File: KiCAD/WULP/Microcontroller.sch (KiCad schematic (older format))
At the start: 17 parts

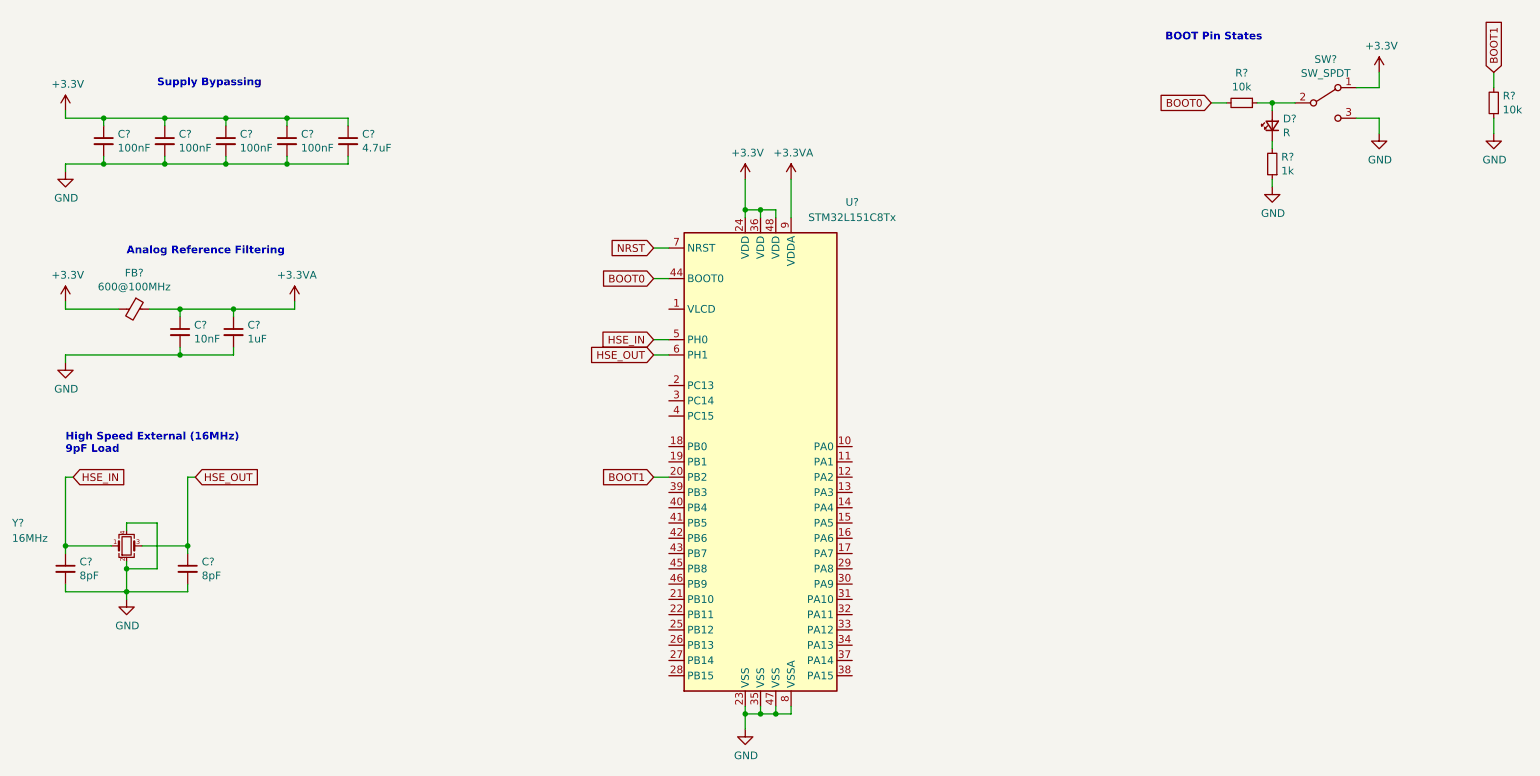
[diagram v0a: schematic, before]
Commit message: WULP sensor/connector updates
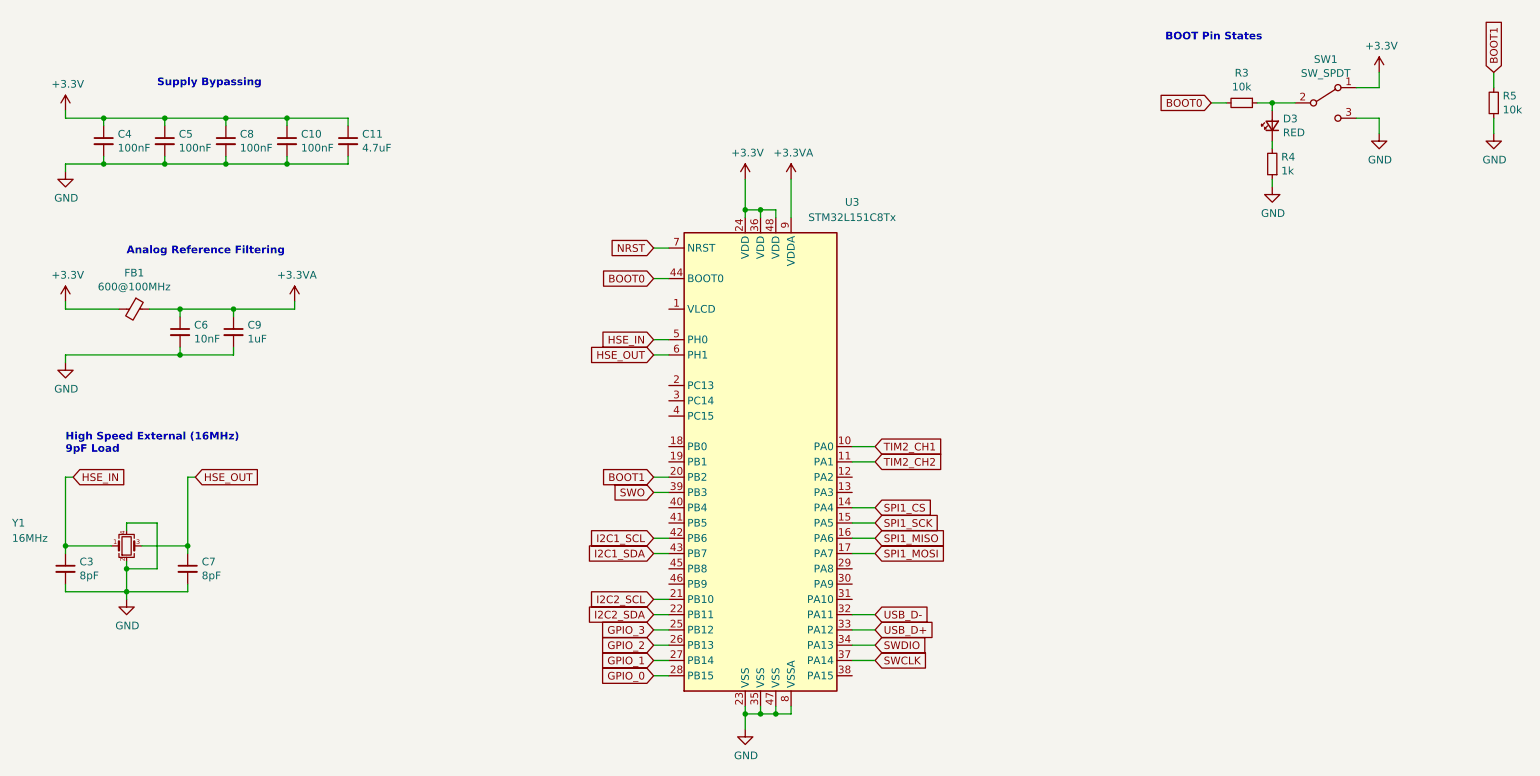
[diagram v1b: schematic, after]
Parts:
- D3: renamed from D?; value R -> RED
- SW1: renamed from SW?; footprint (none) -> Button_Switch_SMD:SW_SPDT_PCM12; LCSC (none) -> C431541
- gave numbers to parts that had none: 15
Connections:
- net TIM2_CH1: now reaches U3.10 (PA0)
- net TIM2_CH2: now reaches U3.11 (PA1)
- net SPI1_CS: now reaches U3.14 (PA4)
- net SPI1_SCK: now reaches U3.15 (PA5)
- net SPI1_MISO: now reaches U3.16 (PA6)
- net SPI1_MOSI: now reaches U3.17 (PA7)
- net I2C2_SCL: now reaches U3.21 (PB10)
- net I2C2_SDA: now reaches U3.22 (PB11)
- net GPIO_3: now reaches U3.25 (PB12)
- net GPIO_2: now reaches U3.26 (PB13)
- net GPIO_1: now reaches U3.27 (PB14)
- net GPIO_0: now reaches U3.28 (PB15)
- net USB_D-: now reaches U3.32 (PA11)
- net USB_D+: now reaches U3.33 (PA12)
- net SWDIO: now reaches U3.34 (PA13)
- net SWCLK: now reaches U3.37 (PA14)
- net SWO: now reaches U3.39 (PB3)
- net I2C1_SCL: now reaches U3.42 (PB6)
- net I2C1_SDA: now reaches U3.43 (PB7)
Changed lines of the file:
@@
 $Descr A4 11693 8268
 encoding utf-8
-Sheet 3 3
+Sheet 3 5
 Title ""
 Date ""
@@
 $EndDescr
 $Comp
-L MCU_ST_STM32L1:STM32L151C8Tx U?
+L MCU_ST_STM32L1:STM32L151C8Tx U3
 U 1 1 61B53E29
 P 5750 3450
-F 0 "U?" H 6350 5150 50  0000 C CNN
+F 0 "U3" H 6350 5150 50  0000 C CNN
 F 1 "STM32L151C8Tx" H 6350 5050 50  0000 C CNN
 F 2 "Package_QFP:LQFP-48_7x7mm_P0.5mm" H 5250 1950 50  0001 R CNN
@@
 $EndComp
 $Comp
-L Device:C_Small C?
+L Device:C_Small C4
 U 1 1 61B55765
 P 1450 1350
-F 0 "C?" H 1542 1396 50  0000 L CNN
+F 0 "C4" H 1542 1396 50  0000 L CNN
 F 1 "100nF" H 1542 1305 50  0000 L CNN
 F 2 "" H 1450 1350 50  0001 C CNN
@@
 $EndComp
 $Comp
-L Device:C_Small C?
+L Device:C_Small C5
 U 1 1 61B56E07
 P 1850 1350
-F 0 "C?" H 1942 1396 50  0000 L CNN
+F 0 "C5" H 1942 1396 50  0000 L CNN
 F 1 "100nF" H 1942 1305 50  0000 L CNN
 F 2 "" H 1850 1350 50  0001 C CNN
@@
 $EndComp
 $Comp
-L Device:C_Small C?
+L Device:C_Small C8
 U 1 1 61B57112
 P 2250 1350
-F 0 "C?" H 2342 1396 50  0000 L CNN
+F 0 "C8" H 2342 1396 50  0000 L CNN
 F 1 "100nF" H 2342 1305 50  0000 L CNN
 F 2 "" H 2250 1350 50  0001 C CNN
@@
 $EndComp
 $Comp
-L Device:C_Small C?
+L Device:C_Small C10
 U 1 1 61B572C5
 P 2650 1350
-F 0 "C?" H 2742 1396 50  0000 L CNN
+F 0 "C10" H 2742 1396 50  0000 L CNN
 F 1 "100nF" H 2742 1305 50  0000 L CNN
 F 2 "" H 2650 1350 50  0001 C CNN
@@
 $EndComp
 $Comp
-L Device:C_Small C?
+L Device:C_Small C11
 U 1 1 61B57637
 P 3050 1350
-F 0 "C?" H 3142 1396 50  0000 L CNN
+F 0 "C11" H 3142 1396 50  0000 L CNN
 F 1 "4.7uF" H 3142 1305 50  0000 L CNN
 F 2 "" H 3050 1350 50  0001 C CNN
@@
 $EndComp
 $Comp
-L power:+3.3V #PWR?
+L power:+3.3V #PWR0114
 U 1 1 61B57B0B
 P 1200 1150
-F 0 "#PWR?" H 1200 1000 50  0001 C CNN
+F 0 "#PWR0114" H 1200 1000 50  0001 C CNN
 F 1 "+3.3V" H 1215 1323 50  0000 C CNN
 F 2 "" H 1200 1150 50  0001 C CNN
@@
 $EndComp
 $Comp
-L power:GND #PWR?
+L power:GND #PWR0115
 U 1 1 61B58427
 P 1200 1550
-F 0 "#PWR?" H 1200 1300 50  0001 C CNN
+F 0 "#PWR0115" H 1200 1300 50  0001 C CNN
 F 1 "GND" H 1205 1377 50  0000 C CNN
 F 2 "" H 1200 1550 50  0001 C CNN
@@
 	1450 1500 1850 1500
 $Comp
-L power:+3.3V #PWR?
+L power:+3.3V #PWR0116
 U 1 1 61B59DEE
 P 5650 1600
-F 0 "#PWR?" H 5650 1450 50  0001 C CNN
+F 0 "#PWR0116" H 5650 1450 50  0001 C CNN
 F 1 "+3.3V" H 5665 1773 50  0000 C CNN
 F 2 "" H 5650 1600 50  0001 C CNN
@@
 Connection ~ 5750 1800
 $Comp
-L power:+3.3VA #PWR?
+L power:+3.3VA #PWR0117
 U 1 1 61B5BA93
 P 5950 1600
-F 0 "#PWR?" H 5950 1450 50  0001 C CNN
+F 0 "#PWR0117" H 5950 1450 50  0001 C CNN
 F 1 "+3.3VA" H 5965 1773 50  0000 C CNN
 F 2 "" H 5950 1600 50  0001 C CNN
@@
 	5950 1600 5950 1850
 $Comp
-L power:+3.3V #PWR?
+L power:+3.3V #PWR0118
 U 1 1 61B5C7AD
 P 1200 2400
-F 0 "#PWR?" H 1200 2250 50  0001 C CNN
+F 0 "#PWR0118" H 1200 2250 50  0001 C CNN
 F 1 "+3.3V" H 1215 2573 50  0000 C CNN
 F 2 "" H 1200 2400 50  0001 C CNN
@@
 $EndComp
 $Comp
-L power:GND #PWR?
+L power:GND #PWR0119
 U 1 1 61B5CCD8
 P 1200 2800
-F 0 "#PWR?" H 1200 2550 50  0001 C CNN
+F 0 "#PWR0119" H 1200 2550 50  0001 C CNN
 F 1 "GND" H 1205 2627 50  0000 C CNN
 F 2 "" H 1200 2800 50  0001 C CNN
@@
 $EndComp
 $Comp
-L Device:C_Small C?
+L Device:C_Small C6
 U 1 1 61B5D317
 P 1950 2600
-F 0 "C?" H 2042 2646 50  0000 L CNN
+F 0 "C6" H 2042 2646 50  0000 L CNN
 F 1 "10nF" H 2042 2555 50  0000 L CNN
 F 2 "" H 1950 2600 50  0001 C CNN
@@
 $EndComp
 $Comp
-L Device:C_Small C?
+L Device:C_Small C9
 U 1 1 61B5DC0A
 P 2300 2600
-F 0 "C?" H 2392 2646 50  0000 L CNN
+F 0 "C9" H 2392 2646 50  0000 L CNN
 F 1 "1uF" H 2392 2555 50  0000 L CNN
 F 2 "" H 2300 2600 50  0001 C CNN
@@
 $EndComp
 $Comp
-L power:+3.3VA #PWR?
+L power:+3.3VA #PWR0120
 U 1 1 61B5F121
 P 2700 2400
-F 0 "#PWR?" H 2700 2250 50  0001 C CNN
+F 0 "#PWR0120" H 2700 2250 50  0001 C CNN
 F 1 "+3.3VA" H 2715 2573 50  0000 C CNN
 F 2 "" H 2700 2400 50  0001 C CNN
@@
 $EndComp
 $Comp
-L Device:Ferrite_Bead_Small FB?
+L Device:Ferrite_Bead_Small FB1
 U 1 1 61B5FB4B
 P 1650 2450
-F 0 "FB?" V 1413 2450 50  0000 C CNN
+F 0 "FB1" V 1413 2450 50  0000 C CNN
 F 1 "600@100MHz" V 1504 2450 50  0000 C CNN
 F 2 "" V 1580 2450 50  0001 C CNN
@@
 	1950 2750 2300 2750
 $Comp
-L power:GND #PWR?
+L power:GND #PWR0121
 U 1 1 61B65960
 P 5650 5200
-F 0 "#PWR?" H 5650 4950 50  0001 C CNN
+F 0 "#PWR0121" H 5650 4950 50  0001 C CNN
 F 1 "GND" H 5655 5027 50  0000 C CNN
 F 2 "" H 5650 5200 50  0001 C CNN
@@
 Analog Reference Filtering
 $Comp
-L Device:Crystal_GND24_Small Y?
+L Device:Crystal_GND24_Small Y1
 U 1 1 61B82FD5
 P 1600 4000
-F 0 "Y?" H 850 4150 50  0000 L CNN
+F 0 "Y1" H 850 4150 50  0000 L CNN
 F 1 "16MHz" H 850 4050 50  0000 L CNN
 F 2 "Oscillator:Oscillator_SMD_SeikoEpson_SG8002CE-4Pin_3.2x2.5mm" H 1600 4000 50  0001 C CNN
@@
 	1600 4150 1600 4100
 $Comp
-L power:GND #PWR?
+L power:GND #PWR0122
 U 1 1 61B84FE3
 P 1600 4350
-F 0 "#PWR?" H 1600 4100 50  0001 C CNN
+F 0 "#PWR0122" H 1600 4100 50  0001 C CNN
 F 1 "GND" H 1605 4177 50  0000 C CNN
 F 2 "" H 1600 4350 50  0001 C CNN
@@
 	5050 2650 5150 2650
 $Comp
-L Device:C_Small C?
+L Device:C_Small C3
 U 1 1 61B8880B
 P 1200 4150
-F 0 "C?" H 1292 4196 50  0000 L CNN
+F 0 "C3" H 1292 4196 50  0000 L CNN
 F 1 "8pF" H 1292 4105 50  0000 L CNN
 F 2 "" H 1200 4150 50  0001 C CNN
@@
 $EndComp
 $Comp
-L Device:C_Small C?
+L Device:C_Small C7
 U 1 1 61B89170
 P 2000 4150
-F 0 "C?" H 2092 4196 50  0000 L CNN
+F 0 "C7" H 2092 4196 50  0000 L CNN
 F 1 "8pF" H 2092 4105 50  0000 L CNN
 F 2 "" H 2000 4150 50  0001 C CNN
@@
 	5150 3550 5050 3550
 $Comp
-L Switch:SW_SPDT SW?
+L Switch:SW_SPDT SW1
 U 1 1 61BA3EF0
 P 9450 1100
-F 0 "SW?" H 9450 1385 50  0000 C CNN
+F 0 "SW1" H 9450 1385 50  0000 C CNN
 F 1 "SW_SPDT" H 9450 1294 50  0000 C CNN
-F 2 "" H 9450 1100 50  0001 C CNN
+F 2 "Button_Switch_SMD:SW_SPDT_PCM12" H 9450 1100 50  0001 C CNN
 F 3 "~" H 9450 1100 50  0001 C CNN
+F 4 "C431541" H 9450 1100 50  0001 C CNN "LCSC"
 	1    9450 1100
 	1    0    0    -1
@@
 BOOT0
 $Comp
-L Device:R_Small R?
+L Device:R_Small R3
 U 1 1 61BA68DC
 P 8900 1100
-F 0 "R?" V 8704 1100 50  0000 C CNN
+F 0 "R3" V 8704 1100 50  0000 C CNN
 F 1 "10k" V 8795 1100 50  0000 C CNN
 F 2 "" H 8900 1100 50  0001 C CNN
@@
 	9000 1100 9100 1100
 $Comp
-L power:+3.3V #PWR?
+L power:+3.3V #PWR0123
 U 1 1 61BAA6FF
 P 9800 900
-F 0 "#PWR?" H 9800 750 50  0001 C CNN
+F 0 "#PWR0123" H 9800 750 50  0001 C CNN
 F 1 "+3.3V" H 9815 1073 50  0000 C CNN
 F 2 "" H 9800 900 50  0001 C CNN
@@
 $EndComp
 $Comp
-L power:GND #PWR?
+L power:GND #PWR0124
 U 1 1 61BAB201
 P 9800 1300
-F 0 "#PWR?" H 9800 1050 50  0001 C CNN
+F 0 "#PWR0124" H 9800 1050 50  0001 C CNN
 F 1 "GND" H 9805 1127 50  0000 C CNN
 F 2 "" H 9800 1300 50  0001 C CNN
@@
 BOOT1
 $Comp
-L Device:R_Small R?
+L Device:R_Small R5
 U 1 1 61BAF705
 P 10550 1100
-F 0 "R?" H 10491 1054 50  0000 R CNN
+F 0 "R5" H 10491 1054 50  0000 R CNN
 F 1 "10k" H 10491 1145 50  0000 R CNN
 F 2 "" H 10550 1100 50  0001 C CNN
@@
 $EndComp
 $Comp
-L power:GND #PWR?
+L power:GND #PWR0125
 U 1 1 61BAFAE7
 P 10550 1300
-F 0 "#PWR?" H 10550 1050 50  0001 C CNN
+F 0 "#PWR0125" H 10550 1050 50  0001 C CNN
 F 1 "GND" H 10555 1127 50  0000 C CNN
 F 2 "" H 10550 1300 50  0001 C CNN
@@
 	10550 1000 10550 900
 $Comp
-L Device:LED_Small D?
+L Device:LED_Small D3
 U 1 1 61BB391F
 P 9100 1250
-F 0 "D?" V 9146 1180 50  0000 R CNN
-F 1 "R" V 9055 1180 50  0000 R CNN
+F 0 "D3" V 9146 1180 50  0000 R CNN
+F 1 "RED" V 9055 1180 50  0000 R CNN
 F 2 "" V 9100 1250 50  0001 C CNN
 F 3 "~" V 9100 1250 50  0001 C CNN
@@
 $EndComp
 $Comp
-L Device:R_Small R?
+L Device:R_Small R4
 U 1 1 61BB464B
 P 9100 1500
-F 0 "R?" H 9041 1454 50  0000 R CNN
+F 0 "R4" H 9041 1454 50  0000 R CNN
 F 1 "1k" H 9041 1545 50  0000 R CNN
 F 2 "" H 9100 1500 50  0001 C CNN
@@
 $EndComp
 $Comp
-L power:GND #PWR?
+L power:GND #PWR0126
 U 1 1 61BB4BC9
 P 9100 1650
-F 0 "#PWR?" H 9100 1400 50  0001 C CNN
+F 0 "#PWR0126" H 9100 1400 50  0001 C CNN
 F 1 "GND" H 9105 1477 50  0000 C CNN
 F 2 "" H 9100 1650 50  0001 C CNN
@@
 Wire Wire Line
 	5050 2050 5150 2050
+Text GLabel 6500 4450 2    50   Input ~ 0
+USB_D-
+Text GLabel 6500 4550 2    50   Input ~ 0
+USB_D+
+Wire Wire Line
+	6350 4550 6500 4550
+Wire Wire Line
+	6350 4450 6500 4450
+Text GLabel 5050 4350 0    50   Input ~ 0
+I2C2_SCL
+Text GLabel 5050 4450 0    50   Input ~ 0
+I2C2_SDA
+Wire Wire Line
+	5150 4350 5050 4350
+Wire Wire Line
+	5050 4450 5150 4450
+Text GLabel 6500 3750 2    50   Input ~ 0
+SPI1_CS
+Text GLabel 6500 3850 2    50   Input ~ 0
+SPI1_SCK
+Text GLabel 6500 3950 2    50   Input ~ 0
+SPI1_MISO
+Text GLabel 6500 4050 2    50   Input ~ 0
+SPI1_MOSI
+Text GLabel 6500 3350 2    50   Input ~ 0
+TIM2_CH1
+Text GLabel 6500 3450 2    50   Input ~ 0
+TIM2_CH2
+Wire Wire Line
+	6500 3350 6350 3350
+Wire Wire Line
+	6350 3450 6500 3450
+Wire Wire Line
+	6500 3750 6350 3750
+Wire Wire Line
+	6350 3850 6500 3850
+Wire Wire Line
+	6500 3950 6350 3950
+Wire Wire Line
+	6350 4050 6500 4050
+Text GLabel 5050 3650 0    50   Input ~ 0
+SWO
+Text GLabel 6500 4750 2    50   Input ~ 0
+SWCLK
+Text GLabel 6500 4650 2    50   Input ~ 0
+SWDIO
+Wire Wire Line
+	6350 4650 6500 4650
+Wire Wire Line
+	6350 4750 6500 4750
+Wire Wire Line
+	5150 3650 5050 3650
+Text GLabel 5050 4050 0    50   Input ~ 0
+I2C1_SDA
+Text GLabel 5050 3950 0    50   Input ~ 0
+I2C1_SCL
+Wire Wire Line
+	5150 3950 5050 3950
+Wire Wire Line
+	5050 4050 5150 4050
+Text GLabel 5050 4550 0    50   Input ~ 0
+GPIO_3
+Text GLabel 5050 4650 0    50   Input ~ 0
+GPIO_2
+Text GLabel 5050 4750 0    50   Input ~ 0
+GPIO_1
+Text GLabel 5050 4850 0    50   Input ~ 0
+GPIO_0
+Wire Wire Line
+	5050 4550 5150 4550
+Wire Wire Line
+	5150 4650 5050 4650
+Wire Wire Line
+	5050 4750 5150 4750
+Wire Wire Line
+	5150 4850 5050 4850
 $EndSCHEMATC
